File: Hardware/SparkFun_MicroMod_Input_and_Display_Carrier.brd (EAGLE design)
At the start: 57.1 x 82.5 mm, 103 parts, among them J1 MICROMOD-2222-C, J2 MICRO-SD, J3 USB-C_Prog, J4 AVR_SPI_PROG_3X2TESTPOINTS, J5 2.4" TFT, J6 QWIIC_RA, J7 CORTEX_JTAG_DEBUG, Q1 1.1A/600mΩ, U2 ATTINY84, U5 AP7361C-33FGE

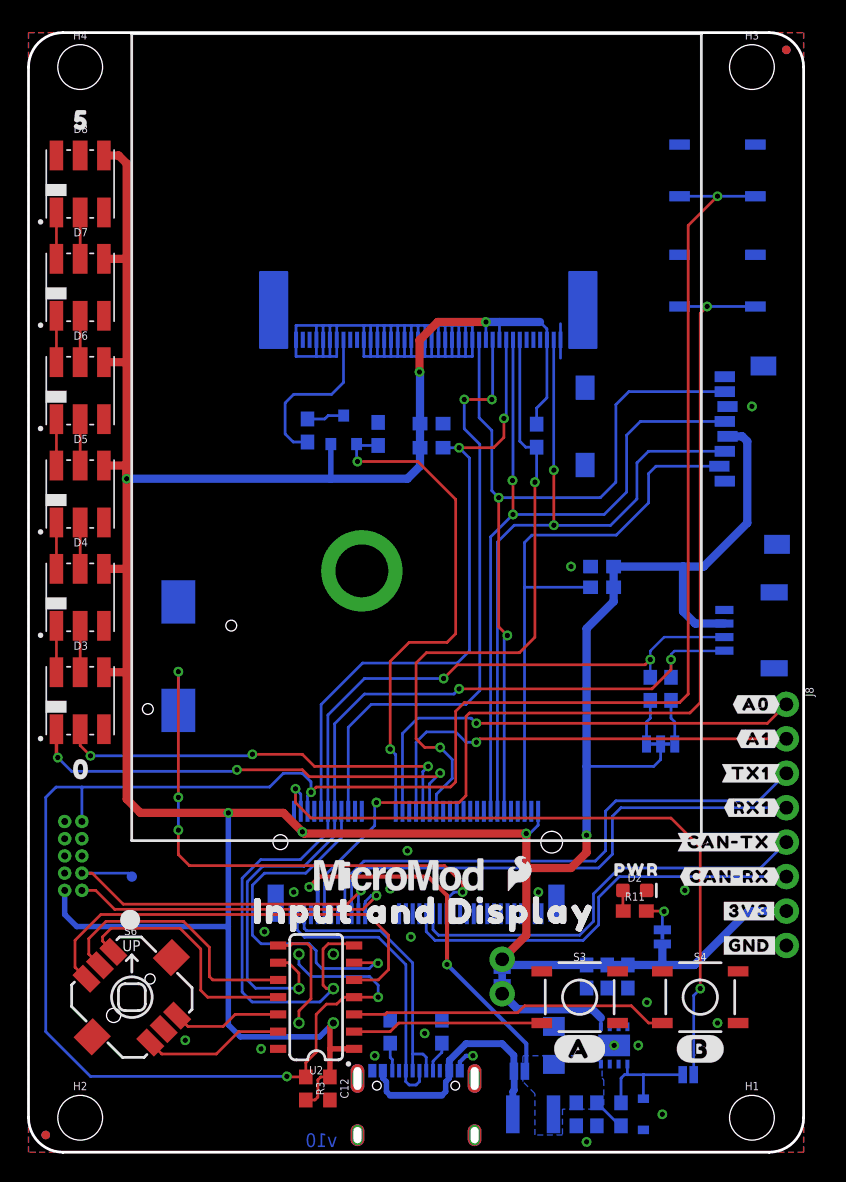
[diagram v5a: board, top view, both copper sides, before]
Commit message: v10 post review changes
-Added 5V/V_USB pin
-Added BJT to buzzer
-Replaced pull up/down resistors from 10lk to 100k
-Replaced 1/10W 10ohm resistor with 1/4W 10ohm
-Removed display outline on tPlace layer
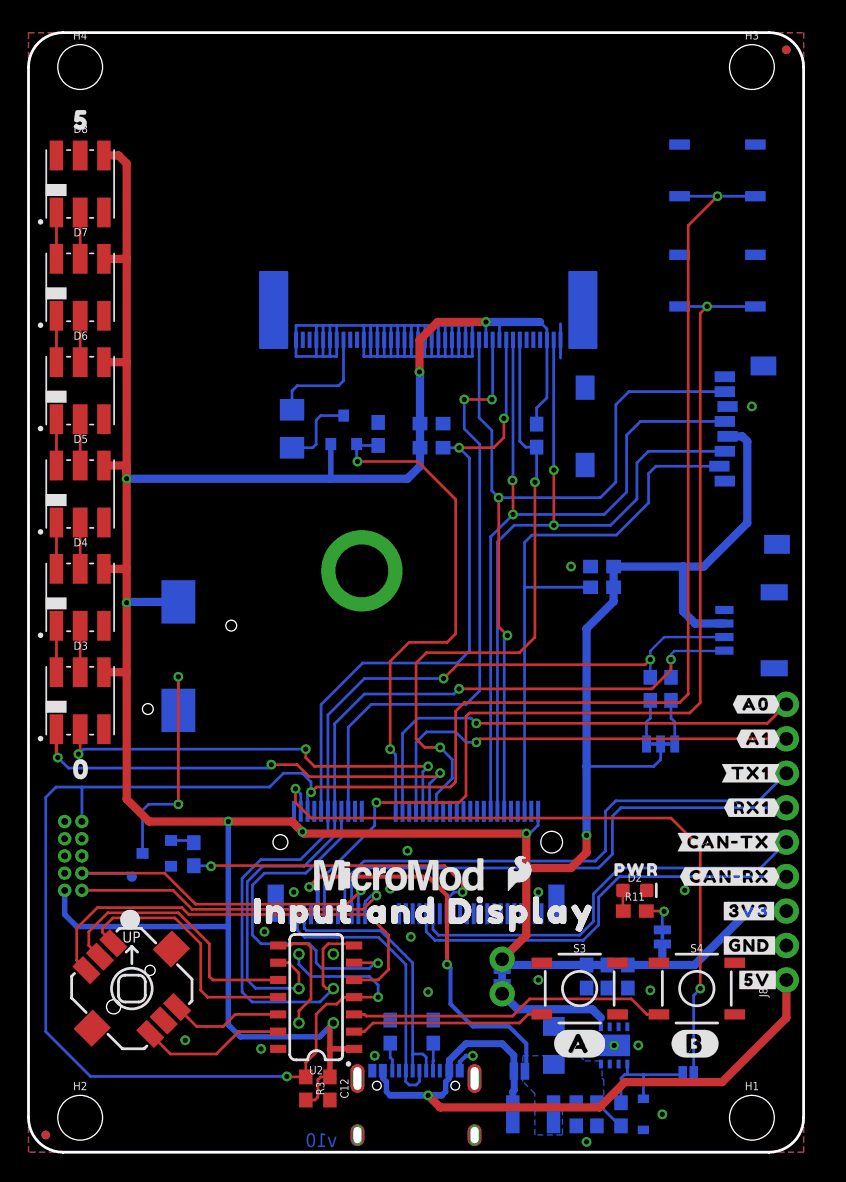
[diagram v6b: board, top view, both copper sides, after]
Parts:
- added Q2: 600mA/40V, SparkFun-DiscreteSemi:SOT23-3
- added R13: 1k, SparkFun-Resistors:0603
- added U$18, U$38: (no value), output:#5V#0
- J8: device SparkFun-Connectors:1X08_NO_SILK -> SparkFun-Connectors:1X09_NO_SILK
- R10, R3, R4, R6, R9: value 10k -> 100k
- R12: device SparkFun-Resistors:0603 -> SparkFun-Resistors:1206
- moved J8 20.3 mm to (55.9, 12.7), turned to 90 degrees
- moved R12 1.15 mm to (19.4, 53.3), turned to 270 degrees
- moved S4 0.68 mm to (49.3, 12.1)
- moved R2 0.64 mm to (29.8, 8.89)
- moved S3 0.63 mm to (40.6, 12.1)
- moved S6 0.63 mm to (7.62, 12.1)
- moved U$6 0.54 mm to (49.1, 8.00)
- moved U$5 0.38 mm to (40.6, 8.00)
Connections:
- new net N$5: LS1.-, Q2.3
- new net N$6: Q2.1, R13.2
- net 3.3V: now also J8.3, LS1.+; no longer J8.7
- net A0: now also J8.9; no longer J8.1
- net A1: now also J8.8; no longer J8.2
- net BUZZER: now also R13.1; no longer LS1.-
- net CAN-RX: now also J8.4; no longer J8.6
- net GND: now also J8.2, Q2.2; no longer J8.8, LS1.+
- net RX1: now also J8.6; no longer J8.4
- net TX1: now also J8.7; no longer J8.3
- net V_USB: now also J8.1
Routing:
- net V_USB: track 18.7 -> 51.0 mm, vias 0 -> 1
- net N$5: track 0.00 -> 17.9 mm, vias 0 -> 2
- net BUZZER: track 41.3 -> 23.5 mm, vias 4 -> 2
- net N$3: track 12.3 -> 8.52 mm
- net 3.3V: track 288.5 -> 291.7 mm, vias 7 -> 8
- net N$4: track 2.77 -> 5.83 mm
- net N$6: track 0.00 -> 1.75 mm
- net VIN: track 31.4 -> 33.0 mm
- net LED_CLK: track 31.1 -> 32.2 mm
- net BTN_UP: track 18.5 -> 19.1 mm

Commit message: v10 cleanup
-Updated active low labels
-Fixed Attiny I2C address
-Updated measures layer
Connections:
- net DISP_!CS renamed !DISP_CS
- net DISP_!RST renamed !DISP_RST
- net DISP_BL renamed !DISP_BL
- net SD_!CS renamed !SD_CS
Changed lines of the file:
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@@
 <layer number="50" name="dxf" color="7" fill="1" visible="no" active="yes"/>
 <layer number="51" name="tDocu" color="6" fill="1" visible="yes" active="yes"/>
-<layer number="52" name="bDocu" color="7" fill="1" visible="yes" active="yes"/>
+<layer number="52" name="bDocu" color="7" fill="1" visible="no" active="yes"/>
 <layer number="91" name="Nets" color="2" fill="1" visible="no" active="no"/>
 <layer number="92" name="Busses" color="1" fill="1" visible="no" active="no"/>
@@
 <text x="38.354" y="-23.495" size="1.778" layer="51" font="vector" align="center">Alex Wende</text>
 <dimension x1="0" y1="0" x2="57.15" y2="0" x3="28.575" y3="-10.16" textsize="1.778" layer="47" unit="inch" visible="yes"/>
-<dimension x1="7.62" y1="11.43" x2="0" y2="11.43" x3="3.81" y3="-3.81" textsize="1.778" layer="47" unit="inch"/>
-<dimension x1="7.62" y1="11.43" x2="7.62" y2="0" x3="-2.54" y3="5.715" textsize="1.778" layer="47" unit="inch"/>
-<dimension x1="31.75" y1="11.43" x2="49.53" y2="11.43" x3="40.64" y3="-3.81" textsize="1.778" layer="47" unit="inch"/>
-<dimension x1="49.53" y1="11.43" x2="57.15" y2="11.43" x3="53.34" y3="-3.81" textsize="1.778" layer="47" unit="inch"/>
-<dimension x1="31.75" y1="11.43" x2="7.62" y2="11.43" x3="19.685" y3="-3.81" textsize="1.778" layer="47" unit="inch"/>
+<dimension x1="7.62" y1="12.065" x2="0" y2="12.065" x3="3.81" y3="-3.175" textsize="1.778" layer="47" unit="inch"/>
+<dimension x1="7.62" y1="12.065" x2="7.62" y2="0" x3="-2.54" y3="6.0325" textsize="1.778" layer="47" unit="inch" precision="3"/>
+<dimension x1="40.64" y1="12.065" x2="49.276" y2="12.065" x3="44.958" y3="-3.175" textsize="1.778" layer="47" unit="inch"/>
+<dimension x1="49.276" y1="12.065" x2="57.15" y2="12.065" x3="53.213" y3="-3.174996875" textsize="1.778" layer="47" unit="inch"/>
+<dimension x1="40.64" y1="12.065" x2="7.62" y2="12.065" x3="24.13" y3="-3.175" textsize="1.778" layer="47" unit="inch"/>
 <dimension x1="0" y1="0" x2="0" y2="82.55" x3="-6.35" y3="41.275" textsize="1.778" layer="47" unit="inch"/>
 <dimension x1="3.81" y1="80.01" x2="3.81" y2="82.55" x3="-2.54" y3="81.28" textsize="1.778" layer="47" unit="inch"/>
@@
 <vertex x="7.493" y="16.51" curve="90"/>
 </polygon>
+<dimension x1="49.276" y1="12.065" x2="49.276" y2="0" x3="62.23" y3="6.0325" textsize="1.778" textratio="15" layer="47" unit="inch" precision="3"/>
 </plain>
 <attributes>
@@
 <wire x1="44.269" y1="56.08" x2="43.307" y2="55.118" width="0.2032" layer="16"/>
 </signal>
-<signal name="SD_!CS">
+<signal name="!SD_CS">
 <contactref element="J1" pad="70"/>
 <contactref element="J2" pad="CS"/>
@@
 <wire x1="43.341" y1="45.5" x2="37.118" y2="45.5" width="0.2032" layer="16"/>
 </signal>
-<signal name="DISP_!CS">
+<signal name="!DISP_CS">
 <contactref element="J1" pad="10"/>
 <contactref element="J5" pad="32"/>
@@
 <wire x1="25.273" y1="33.02" x2="23.575" y2="31.322" width="0.2032" layer="16"/>
 </signal>
-<signal name="DISP_BL">
+<signal name="!DISP_BL">
 <contactref element="J1" pad="32"/>
 <wire x1="26.67" y1="29.718" x2="27.075" y2="29.313" width="0.2032" layer="16"/>
@@
 <wire x1="2.06" y1="65.87" x2="2.06" y2="69.29" width="0.2032" layer="1"/>
 </signal>
-<signal name="DISP_!RST">
+<signal name="!DISP_RST">
 <contactref element="J5" pad="34"/>
 <contactref element="J1" pad="44"/>

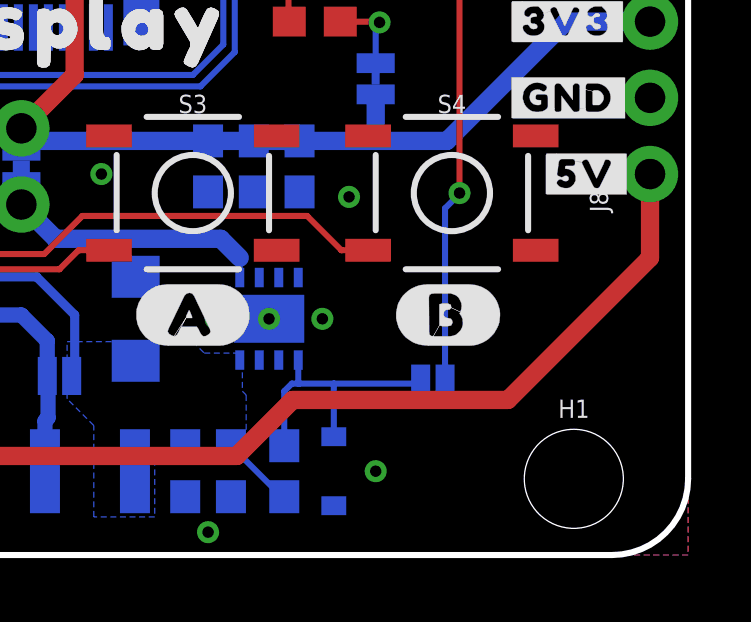
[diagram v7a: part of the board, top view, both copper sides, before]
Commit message: QC fixes
- Added note for MEAS jumper
- Adjusted button B label
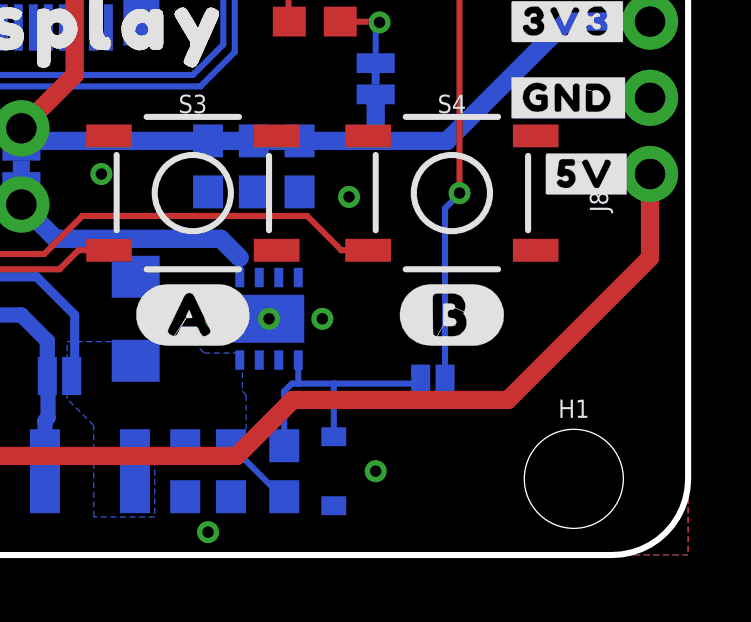
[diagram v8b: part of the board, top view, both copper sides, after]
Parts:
- moved U$6 0.13 mm to (49.3, 8.00)
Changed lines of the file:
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@@
 <element name="U$2" library="output" package="INPUT_AND_DISPLAY0" value="" x="29.21" y="17.78" smashed="yes"/>
 <element name="U$5" library="output" package="#A#0" value="" x="40.64" y="8.001" smashed="yes"/>
-<element name="U$6" library="output" package="#B#0" value="" x="49.149" y="8.001" smashed="yes"/>
+<element name="U$6" library="output" package="#B#0" value="" x="49.276" y="8.001" smashed="yes"/>
 <element name="U$7" library="output" package="00" value="" x="3.937" y="28.21" smashed="yes"/>
 <element name="U$8" library="output" package="50" value="" x="3.937" y="76.089" smashed="yes"/>
